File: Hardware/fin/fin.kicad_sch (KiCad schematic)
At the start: 46 parts, among them J1 Conn_01x10_Pin, J2 Conn_01x04_Pin, J3 Conn_01x04_Pin, J5 Conn_01x04_Pin, U1 ADS131M03QPWRQ1, U2 ADXL380-1BCCZ-RL7, U3 W25N512GVEIG, U4 TMP235A4DBZR, U5 STM32L412K8Ux, U6 ADXL380-1BCCZ-RL7, X1 ECS-327TXO-33-TR

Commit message: oooooooooo we're half way theeerree
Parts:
- removed C17, C18, C9: 0.1uF, Capacitor_SMD:C_0603_1608Metric, symbol Device:C_Small
- removed JP1, JP2, JP3: SolderJumper_3_Open, Jumper:SolderJumper-3_P1.3mm_Open_RoundedPad1.0x1.5mm, symbol Jumper:SolderJumper_3_Open
- added C22, C23: 0.1uF, Capacitor_SMD:C_0402_1005Metric, symbol Device:C_Small
- added C24: 1uF, Capacitor_SMD:C_0402_1005Metric, symbol Device:C_Small
- C1, C10, C11, C12, C13, C14, C15, C16, C19, C2, C20, C3, C4, C5: footprint Capacitor_SMD:C_0603_1608Metric -> Capacitor_SMD:C_0402_1005Metric
- C21: value 0.1uF -> 1uF; footprint Capacitor_SMD:C_0603_1608Metric -> Capacitor_SMD:C_0402_1005Metric
- D1, D4: footprint LED_SMD:LED_0603_1608Metric -> LED_SMD:LED_0402_1005Metric
- R1, R10, R11, R12, R13, R14, R2, R3, R4, R5, R6, R7: footprint Resistor_SMD:R_0603_1608Metric -> Resistor_SMD:R_0402_1005Metric
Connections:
- net +3.3V: now also C23.1, C24.1; no longer C19.2, U2.8 (V1P8), U6.8 (V1P8)
- net ADXL1_CS: now also U6.5 (*CS/ASEL1); no longer U2.5 (*CS/ASEL1)
- net ADXL2_CS: now also U2.5 (*CS/ASEL1); no longer U6.5 (*CS/ASEL1)
- net GND: now also C22.1, C23.2, C24.2
- net QSPI_IO1: now also U3.2 (DO_(IO1))
- net QSPI_IO2: now also U3.3 (/WP_(IO2))
- net QSPI_SCK: now also U3.6 (CLK)
- new net: C22.2, U6.8 (V1P8)
- new net: C19.2, U2.8 (V1P8)
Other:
- note removed: "MISO"
- note removed: "MOSI"

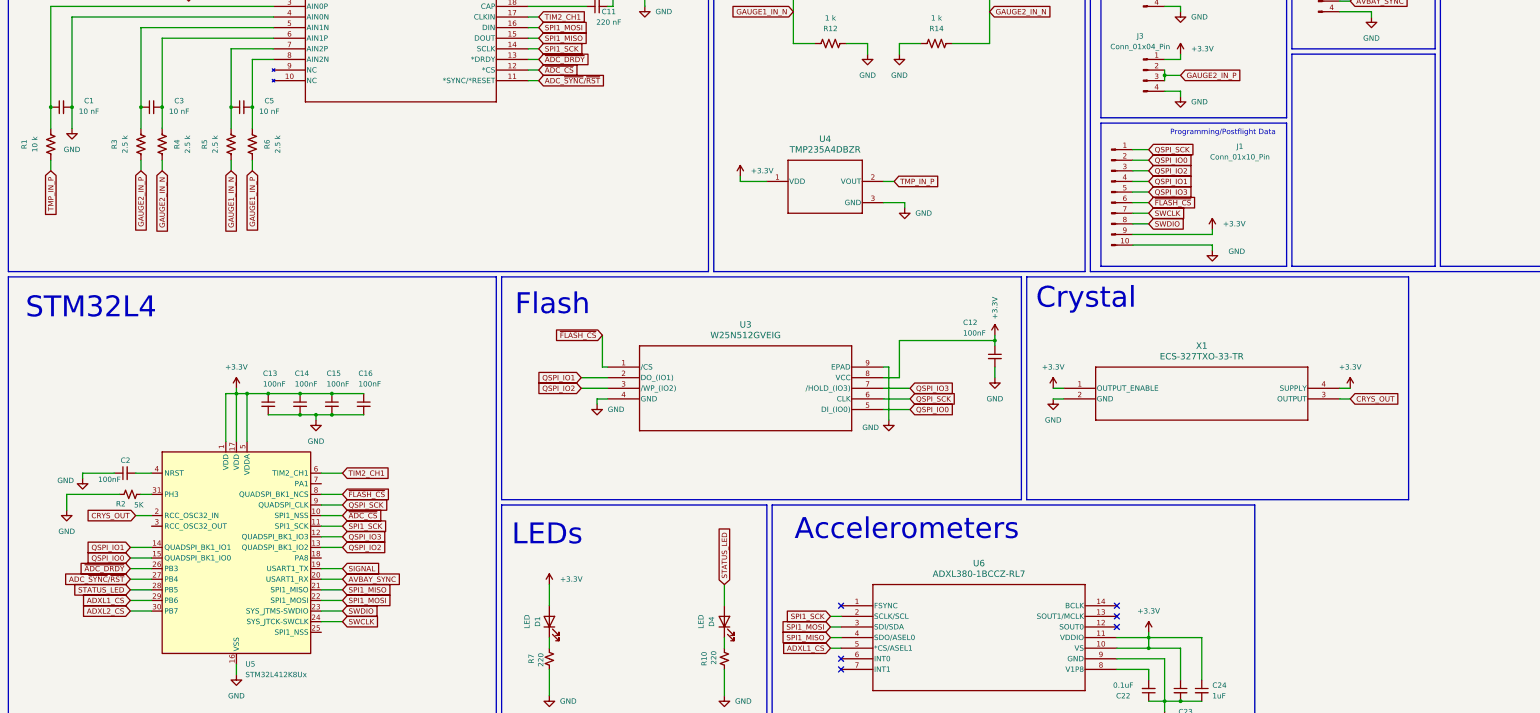
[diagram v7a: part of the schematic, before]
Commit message: some rerouting and soldermask removing
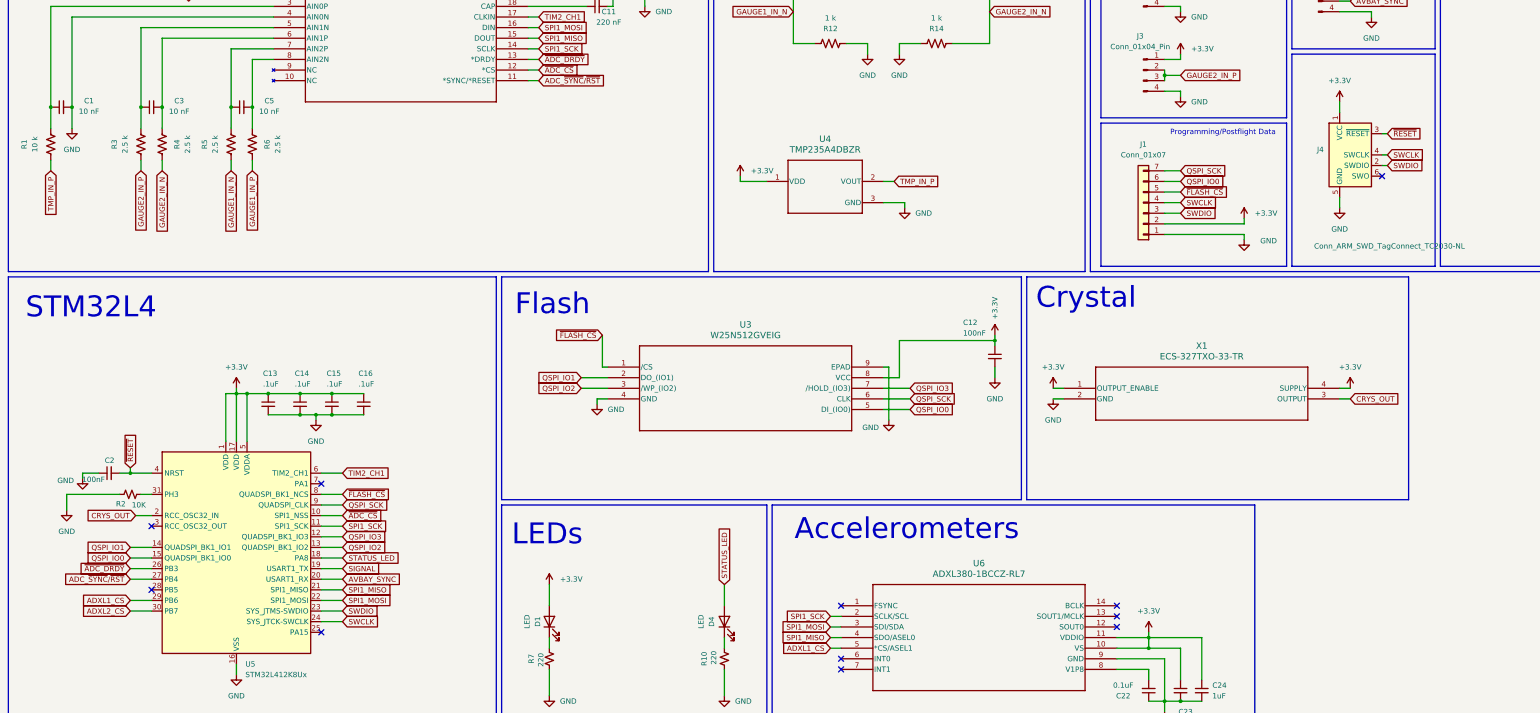
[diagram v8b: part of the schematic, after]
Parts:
- removed J1: Conn_01x10_Pin, Connector_PinHeader_2.54mm:PinHeader_1x10_P2.54mm_Vertical, symbol Connector:Conn_01x10_Pin
- added J1: Conn_01x07, Connector_PinHeader_2.54mm:PinHeader_1x07_P2.54mm_Vertical, symbol Connector_Generic:Conn_01x07
- added J4: Conn_ARM_SWD_TagConnect_TC2030-NL, Connector:Tag-Connect_TC2030-IDC-NL_2x03_P1.27mm_Vertical, symbol Connector:Conn_ARM_SWD_TagConnect_TC2030-NL
- C13, C14, C15, C16: value 100nF -> .1uF
- R2: value 5K -> 10K
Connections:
- net +3.3V: now also J1.2 (Pin_2), J4.1 (VCC)
- net GND: now also J1.1 (Pin_1), J4.5 (GND)
- net QSPI_IO0: now also J1.6 (Pin_6)
- net QSPI_SCK: now also J1.7 (Pin_7)
- net STATUS_LED: now also U5.18 (PA8); no longer U5.28 (PB5)
- net SWCLK: now also J1.4 (Pin_4), J4.4 (SWCLK)
- net SWDIO: now also J1.3 (Pin_3), J4.2 (SWDIO)
- net ~{FLASH_CS}: now also J1.5 (Pin_5)
- net ~{RESET}: now reaches C2.2, U5.4 (NRST)
- net ~{RESET}: now also J4.3 (~{RESET})
- no-connect marks 12 -> 17
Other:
- moved on the sheet: C2
